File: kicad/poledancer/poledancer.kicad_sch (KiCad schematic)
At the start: 36 parts, among them J1 Conn_01x01, J2 Conn_01x02, J3 Conn_02x20_Odd_Even, Q1 MMBT3904, U10 TL074, U11 PS508, U12 M24C02-WMN, U13 PCA9555D, U8 LM4040AIM3-2.5, U9 PS508

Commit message: v0.1 sent to manufacture
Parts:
- C21: LCSC (none) -> C23630
- R75, R83: LCSC C17936 -> C25804
- U13: LCSC C23184 -> C83265
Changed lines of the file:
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@@
       (effects (font (size 1.27 1.27)) hide)
     )
-    (property "LCSC" "C23184" (at 185.42 67.31 0)
+    (property "LCSC" "C83265" (at 185.42 67.31 0)
       (effects (font (size 1.27 1.27)) hide)
     )
@@
       (effects (font (size 1.27 1.27)) hide)
     )
-    (property "LCSC" "" (at 171.45 252.73 0)
+    (property "LCSC" "C23630" (at 171.45 252.73 0)
       (effects (font (size 1.27 1.27)) hide)
     )
@@
       (effects (font (size 1.27 1.27)) hide)
     )
-    (property "LCSC" "C17936" (at 281.94 233.68 0)
+    (property "LCSC" "C25804" (at 281.94 233.68 0)
       (effects (font (size 1.27 1.27)) hide)
     )
@@
       (effects (font (size 1.27 1.27)) hide)
     )
-    (property "LCSC" "C17936" (at 288.29 46.99 0)
-      (effects (font (size 1.27 1.27)) hide)
-    )
+    (property "LCSC" "C25804" (at 288.29 46.99 0)
+      (effects (font (size 1.27 1.27)) hide)
+    )

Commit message: updates to z3340 and poledancer schematics and layout
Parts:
- R52: value 4k7 -> 3k; LCSC C23162 -> C4211
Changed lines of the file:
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@@
       (effects (font (size 1.27 1.27)) (justify left))
     )
-    (property "Value" "4k7" (at 183.388 241.173 0)
+    (property "Value" "3k" (at 183.388 241.173 0)
       (effects (font (size 1.27 1.27)) (justify left))
     )
@@
       (effects (font (size 1.27 1.27)) hide)
     )
-    (property "LCSC" "C23162" (at 181.61 240.03 0)
+    (property "LCSC" "C4211" (at 181.61 240.03 0)
       (effects (font (size 1.27 1.27)) hide)
     )

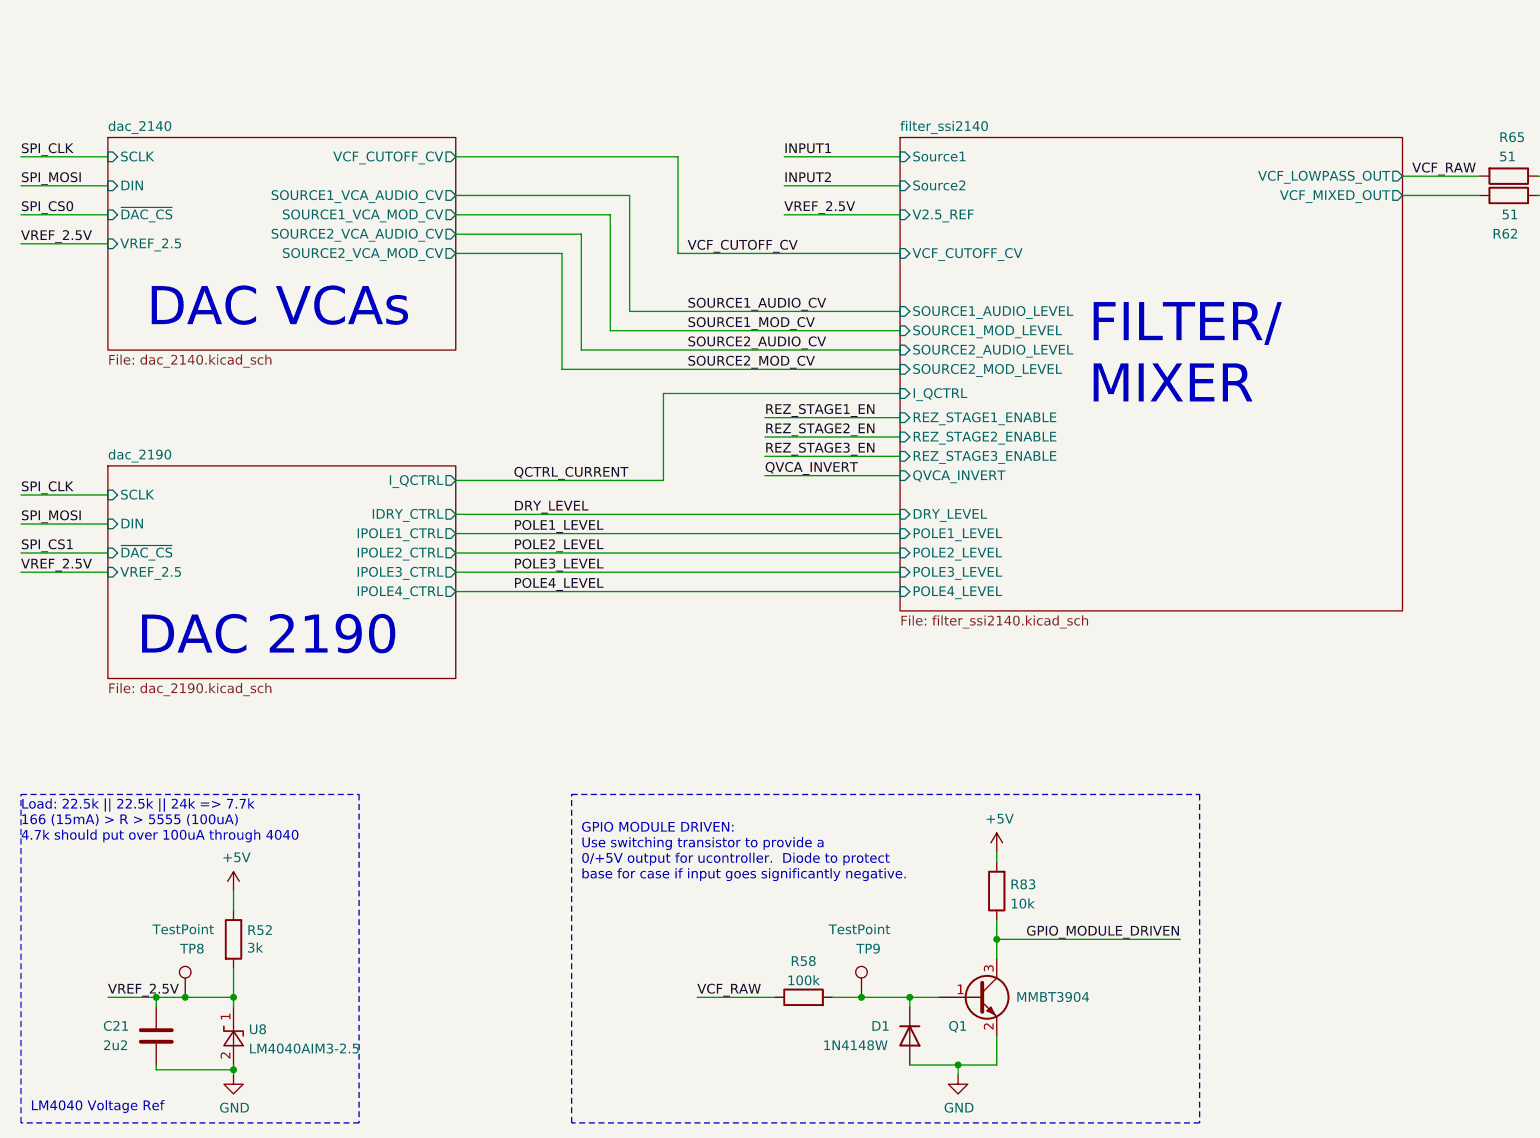
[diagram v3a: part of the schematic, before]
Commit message: add testpoints to DAC2190 for calibration
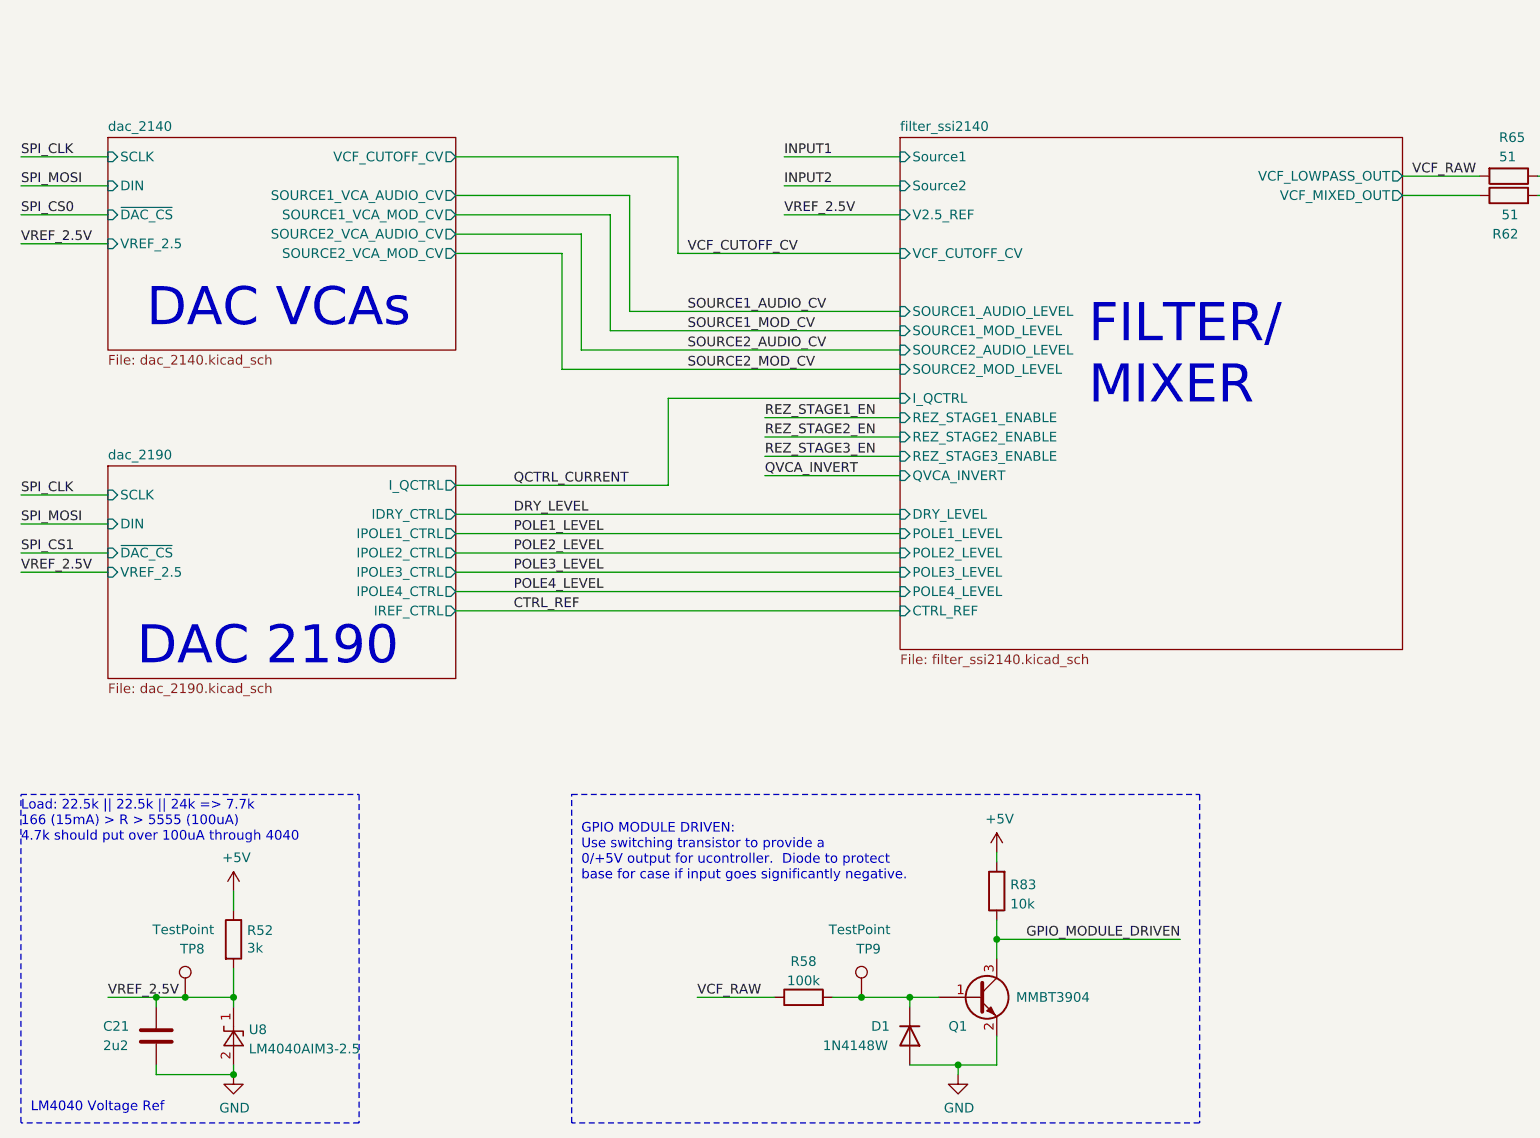
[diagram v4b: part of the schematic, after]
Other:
- sheet dac_2190 ports: added IREF_CTRL; removed none
- sheet filter_ssi2140 ports: added CTRL_REF; removed none
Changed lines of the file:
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@@
   (title_block
     (title "Zoxnoxious Pole Dancer Mixing Filter")
-    (date "2025-02-13")
-    (rev "0.2")
+    (date "2025-11-26")
+    (rev "0.3")
     (company "Zoxnoxious Engineering")
   )
@@
   (junction (at 109.22 81.28) (diameter 0) (color 0 0 0 0)
   )
-  (junction (at 181.61 257.175) (diameter 0) (color 0 0 0 0)
+  (junction (at 181.61 257.81) (diameter 0) (color 0 0 0 0)
   )
   (junction (at 109.22 52.07) (diameter 0) (color 0 0 0 0)
@@
     (stroke (width 0) (type default))
   )
-  (wire (pts (xy 181.61 256.54) (xy 181.61 257.175))
+  (wire (pts (xy 181.61 256.54) (xy 181.61 257.81))
     (stroke (width 0) (type default))
   )
@@
     (stroke (width 0) (type default))
   )
+  (wire (pts (xy 210.82 196.85) (xy 269.24 196.85))
+    (stroke (width 0) (type default))
+  )
   (wire (pts (xy 52.07 166.37) (xy 52.07 168.91))
     (stroke (width 0) (type default))
@@
     (stroke (width 0) (type default))
   )
-  (wire (pts (xy 210.82 179.705) (xy 238.125 179.705))
+  (wire (pts (xy 210.82 180.34) (xy 238.76 180.34))
     (stroke (width 0) (type default))
   )
@@
     (stroke (width 0) (type default))
   )
-  (wire (pts (xy 171.45 257.175) (xy 181.61 257.175))
+  (wire (pts (xy 171.45 257.81) (xy 181.61 257.81))
     (stroke (width 0) (type default))
   )
@@
     (stroke (width 0) (type default))
   )
-  (wire (pts (xy 238.125 168.275) (xy 238.125 179.705))
+  (wire (pts (xy 238.76 168.91) (xy 238.76 180.34))
     (stroke (width 0) (type default))
   )
@@
     (stroke (width 0) (type default))
   )
-  (wire (pts (xy 181.61 257.175) (xy 181.61 257.81))
-    (stroke (width 0) (type default))
-  )
   (wire (pts (xy 210.82 186.69) (xy 269.24 186.69))
     (stroke (width 0) (type default))
@@
     (stroke (width 0) (type default))
   )
-  (wire (pts (xy 171.45 256.54) (xy 171.45 257.175))
+  (wire (pts (xy 171.45 256.54) (xy 171.45 257.81))
     (stroke (width 0) (type default))
   )
@@
     (stroke (width 0) (type default))
   )
-  (wire (pts (xy 269.24 168.275) (xy 238.125 168.275))
+  (wire (pts (xy 269.24 168.91) (xy 238.76 168.91))
     (stroke (width 0) (type default))
   )
@@
     (effects (font (size 1.27 1.27)) (justify left bottom))
   )
-  (text "DAC 2190" (at 168.91 203.2 0)
+  (text "DAC 2190" (at 168.91 204.47 0)
     (effects (font (size 5.0038 5.0038)) (justify left bottom))
   )
@@
     (effects (font (size 1.27 1.27)) (justify left bottom))
   )
-  (label "QCTRL_CURRENT" (at 218.44 179.705 0) (fields_autoplaced)
+  (label "QCTRL_CURRENT" (at 218.44 180.34 0) (fields_autoplaced)
     (effects (font (size 1.27 1.27)) (justify left bottom))
   )
@@
     (effects (font (size 1.27 1.27)) (justify left bottom))
   )
+  (label "CTRL_REF" (at 218.44 196.85 0) (fields_autoplaced)
+    (effects (font (size 1.27 1.27)) (justify left bottom))
+  )
   (label "INPUT1" (at 254 137.16 0) (fields_autoplaced)
     (effects (font (size 1.27 1.27)) (justify left bottom))
@@
       (effects (font (size 1.27 1.27)) (justify left))
     )
-    (pin "I_QCTRL" output (at 210.82 179.705 0)
+    (pin "I_QCTRL" output (at 210.82 180.34 0)
+      (effects (font (size 1.27 1.27)) (justify right))
+    )
+    (pin "IREF_CTRL" output (at 210.82 196.85 0)
       (effects (font (size 1.27 1.27)) (justify right))
     )
@@
     )
   )
-  (sheet (at 269.24 134.62) (size 66.04 62.23) (fields_autoplaced)
+  (sheet (at 269.24 134.62) (size 66.04 67.31) (fields_autoplaced)
     (stroke (width 0.1524) (type solid))
     (fill (color 0 0 0 0.0000))
@@
       (effects (font (size 1.27 1.27)) (justify left bottom))
     )
-    (property "Sheetfile" "filter_ssi2140.kicad_sch" (at 269.24 197.4346 0)
+    (property "Sheetfile" "filter_ssi2140.kicad_sch" (at 269.24 202.5146 0)
       (effects (font (size 1.27 1.27)) (justify left top))
     )
@@
       (effects (font (size 1.27 1.27)) (justify left))
     )
-    (pin "I_QCTRL" input (at 269.24 168.275 180)
+    (pin "I_QCTRL" input (at 269.24 168.91 180)
       (effects (font (size 1.27 1.27)) (justify left))
     )
@@
       (effects (font (size 1.27 1.27)) (justify left))
     )
+    (pin "CTRL_REF" input (at 269.24 196.85 180)
+      (effects (font (size 1.27 1.27)) (justify left))
+    )

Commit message: poledancer v0.3 RTM check
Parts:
- H1, H2, H3, H4: now left out of the parts list
- U8: LCSC C460725 -> C111866
- renumbered TP9 to TP4
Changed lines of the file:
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@@
   )
   (symbol (lib_id "Mechanical:MountingHole") (at 346.71 29.21 0) (unit 1)
-    (in_bom yes) (on_board yes) (dnp no)
+    (in_bom no) (on_board yes) (dnp no)
     (property "Reference" "H4" (at 349.25 28.0416 0)
       (effects (font (size 1.27 1.27)) (justify left))
@@
   )
   (symbol (lib_id "Mechanical:MountingHole") (at 360.68 29.21 0) (unit 1)
-    (in_bom yes) (on_board yes) (dnp no)
+    (in_bom no) (on_board yes) (dnp no)
     (property "Reference" "H3" (at 363.22 28.0416 0)
       (effects (font (size 1.27 1.27)) (justify left))
@@
   )
   (symbol (lib_id "Mechanical:MountingHole") (at 360.68 38.1 0) (unit 1)
-    (in_bom yes) (on_board yes) (dnp no)
+    (in_bom no) (on_board yes) (dnp no)
     (property "Reference" "H1" (at 363.22 36.9316 0)
       (effects (font (size 1.27 1.27)) (justify left))
@@
   )
   (symbol (lib_id "Mechanical:MountingHole") (at 346.71 38.1 0) (unit 1)
-    (in_bom yes) (on_board yes) (dnp no)
+    (in_bom no) (on_board yes) (dnp no)
     (property "Reference" "H2" (at 349.25 36.9316 0)
       (effects (font (size 1.27 1.27)) (justify left))
@@
       (effects (font (size 1.27 1.27) italic) hide)
     )
-    (property "LCSC" "C460725" (at 181.61 252.73 0)
+    (property "LCSC" "C111866" (at 181.61 252.73 0)
       (effects (font (size 1.27 1.27)) hide)
     )
@@
   (symbol (lib_id "Connector:TestPoint") (at 264.16 247.65 0) (unit 1)
     (in_bom yes) (on_board yes) (dnp no)
-    (property "Reference" "TP9" (at 266.7 241.3 0)
+    (property "Reference" "TP4" (at 266.7 241.3 0)
       (effects (font (size 1.27 1.27)) (justify right))
     )
@@
       (project "poledancer"
         (path "/7079bdb0-a00e-4bac-b257-cbcf2c91bbd6"
-          (reference "TP9") (unit 1)
-        )
-      )
+          (reference "TP4") (unit 1)
+        )
+      )
